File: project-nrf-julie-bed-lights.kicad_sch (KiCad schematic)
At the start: 10 parts

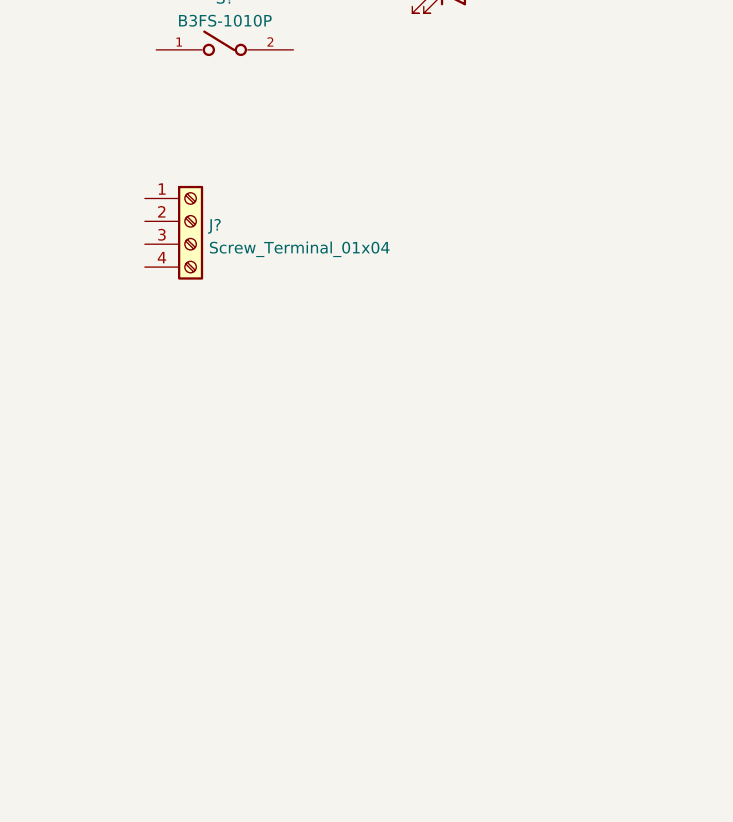
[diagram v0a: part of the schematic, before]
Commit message: Add mounting holes and female sockets
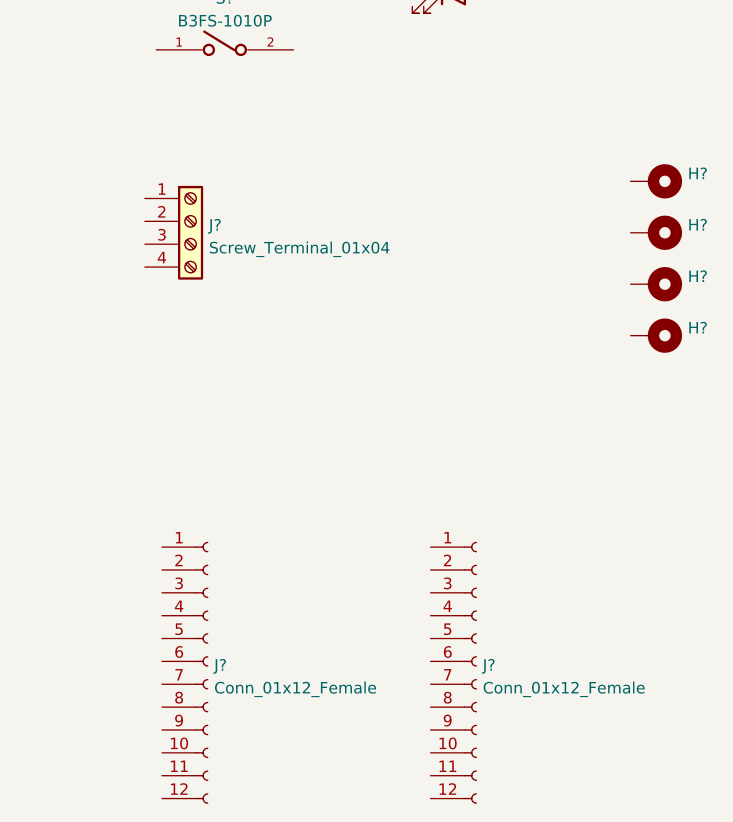
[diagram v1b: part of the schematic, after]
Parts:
- added H? (x4): MountingHole_Pad, MountingHole:MountingHole_2.7mm_M2.5_ISO7380_Pad, symbol Mechanical:MountingHole_Pad
- added J? (x2): Conn_01x12_Female, Connector_PinSocket_2.54mm:PinSocket_1x12_P2.54mm_Vertical_SMD_Pin1Right, symbol Connector:Conn_01x12_Female
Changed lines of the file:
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@@
     (pin "3")
+  )
+  (symbol (lib_id "Mechanical:MountingHole_Pad") (at 149.225 90.17 270) (unit 1)
+    (in_bom yes) (on_board yes) (fields_autoplaced)
+    (property "Reference" "H?" (id 0) (at 153.035 89.3353 90)
+      (effects (font (size 1.27 1.27)) (justify left))
+    )
+    (property "Value" "MountingHole_Pad" (id 1) (at 153.035 91.8722 90)
+      (effects (font (size 1.27 1.27)) (justify left) hide)
+    )
+    (property "Footprint" "MountingHole:MountingHole_2.7mm_M2.5_ISO7380_Pad" (id 2) (at 149.225 90.17 0)
+      (effects (font (size 1.27 1.27)) hide)
+    )
+    (property "Datasheet" "~" (id 3) (at 149.225 90.17 0)
+      (effects (font (size 1.27 1.27)) hide)
+    )
+    (pin "1")
+  )
+  (symbol (lib_id "Connector:Conn_01x12_Female") (at 129.54 137.795 0) (unit 1)
+    (in_bom yes) (on_board yes) (fields_autoplaced)
+    (property "Reference" "J?" (id 0) (at 130.2512 138.2303 0)
+      (effects (font (size 1.27 1.27)) (justify left))
+    )
+    (property "Value" "Conn_01x12_Female" (id 1) (at 130.2512 140.7672 0)
+      (effects (font (size 1.27 1.27)) (justify left))
+    )
+    (property "Footprint" "Connector_PinSocket_2.54mm:PinSocket_1x12_P2.54mm_Vertical_SMD_Pin1Right" (id 2) (at 129.54 137.795 0)
+      (effects (font (size 1.27 1.27)) hide)
+    )
+    (property "Datasheet" "~" (id 3) (at 129.54 137.795 0)
+      (effects (font (size 1.27 1.27)) hide)
+    )
+    (pin "1")
+    (pin "10")
+    (pin "11")
+    (pin "12")
+    (pin "2")
+    (pin "3")
+    (pin "4")
+    (pin "5")
+    (pin "6")
+    (pin "7")
+    (pin "8")
+    (pin "9")
   )
   (symbol (lib_id "Device:LED") (at 127 63.5 0) (unit 1)
@@
     (pin "2")
   )
+  (symbol (lib_id "Mechanical:MountingHole_Pad") (at 149.225 84.455 270) (unit 1)
+    (in_bom yes) (on_board yes) (fields_autoplaced)
+    (property "Reference" "H?" (id 0) (at 153.035 83.6203 90)
+      (effects (font (size 1.27 1.27)) (justify left))
+    )
+    (property "Value" "MountingHole_Pad" (id 1) (at 153.035 86.1572 90)
+      (effects (font (size 1.27 1.27)) (justify left) hide)
+    )
+    (property "Footprint" "MountingHole:MountingHole_2.7mm_M2.5_ISO7380_Pad" (id 2) (at 149.225 84.455 0)
+      (effects (font (size 1.27 1.27)) hide)
+    )
+    (property "Datasheet" "~" (id 3) (at 149.225 84.455 0)
+      (effects (font (size 1.27 1.27)) hide)
+    )
+    (pin "1")
+  )
+  (symbol (lib_id "Mechanical:MountingHole_Pad") (at 149.225 101.6 270) (unit 1)
+    (in_bom yes) (on_board yes) (fields_autoplaced)
+    (property "Reference" "H?" (id 0) (at 153.035 100.7653 90)
+      (effects (font (size 1.27 1.27)) (justify left))
+    )
+    (property "Value" "MountingHole_Pad" (id 1) (at 153.035 103.3022 90)
+      (effects (font (size 1.27 1.27)) (justify left) hide)
+    )
+    (property "Footprint" "MountingHole:MountingHole_2.7mm_M2.5_ISO7380_Pad" (id 2) (at 149.225 101.6 0)
+      (effects (font (size 1.27 1.27)) hide)
+    )
+    (property "Datasheet" "~" (id 3) (at 149.225 101.6 0)
+      (effects (font (size 1.27 1.27)) hide)
+    )
+    (pin "1")
+  )
+  (symbol (lib_id "Mechanical:MountingHole_Pad") (at 149.225 95.885 270) (unit 1)
+    (in_bom yes) (on_board yes) (fields_autoplaced)
+    (property "Reference" "H?" (id 0) (at 153.035 95.0503 90)
+      (effects (font (size 1.27 1.27)) (justify left))
+    )
+    (property "Value" "MountingHole_Pad" (id 1) (at 153.035 97.5872 90)
+      (effects (font (size 1.27 1.27)) (justify left) hide)
+    )
+    (property "Footprint" "MountingHole:MountingHole_2.7mm_M2.5_ISO7380_Pad" (id 2) (at 149.225 95.885 0)
+      (effects (font (size 1.27 1.27)) hide)
+    )
+    (property "Datasheet" "~" (id 3) (at 149.225 95.885 0)
+      (effects (font (size 1.27 1.27)) hide)
+    )
+    (pin "1")
+  )
   (symbol (lib_id "Connector:Screw_Terminal_01x04") (at 97.79 88.9 0) (unit 1)
     (in_bom yes) (on_board yes) (fields_autoplaced)
@@
     (pin "3")
     (pin "4")
+  )
+  (symbol (lib_id "Connector:Conn_01x12_Female") (at 99.695 137.795 0) (unit 1)
+    (in_bom yes) (on_board yes) (fields_autoplaced)
+    (property "Reference" "J?" (id 0) (at 100.4062 138.2303 0)
+      (effects (font (size 1.27 1.27)) (justify left))
+    )
+    (property "Value" "Conn_01x12_Female" (id 1) (at 100.4062 140.7672 0)
+      (effects (font (size 1.27 1.27)) (justify left))
+    )
+    (property "Footprint" "Connector_PinSocket_2.54mm:PinSocket_1x12_P2.54mm_Vertical_SMD_Pin1Right" (id 2) (at 99.695 137.795 0)
+      (effects (font (size 1.27 1.27)) hide)
+    )
+    (property "Datasheet" "~" (id 3) (at 99.695 137.795 0)
+      (effects (font (size 1.27 1.27)) hide)
+    )
+    (pin "1")
+    (pin "10")
+    (pin "11")
+    (pin "12")
+    (pin "2")
+    (pin "3")
+    (pin "4")
+    (pin "5")
+    (pin "6")
+    (pin "7")
+    (pin "8")
+    (pin "9")
   )
   (symbol (lib_id "Device:LED") (at 127 53.34 0) (unit 1)
@@
       (reference "D?") (unit 1) (value "Color") (footprint "LED_SMD:LED_0603_1608Metric")
     )
+    (path "/79a1a979-e26f-4163-9550-e2360d22044b"
+      (reference "H?") (unit 1) (value "MountingHole_Pad") (footprint "MountingHole:MountingHole_2.7mm_M2.5_ISO7380_Pad")
+    )
+    (path "/ad7a890b-9961-45f3-ad0a-47d76a2b459a"
+      (reference "H?") (unit 1) (value "MountingHole_Pad") (footprint "MountingHole:MountingHole_2.7mm_M2.5_ISO7380_Pad")
+    )
+    (path "/b87d5433-df83-465a-b91e-7e1ece85c8fe"
+      (reference "H?") (unit 1) (value "MountingHole_Pad") (footprint "MountingHole:MountingHole_2.7mm_M2.5_ISO7380_Pad")
+    )
+    (path "/d2b03c54-b52a-42dc-b552-8744a7b0080b"
+      (reference "H?") (unit 1) (value "MountingHole_Pad") (footprint "MountingHole:MountingHole_2.7mm_M2.5_ISO7380_Pad")
+    )
     (path "/384cfa91-ee4e-4e2d-8fc4-bda226af1052"
       (reference "J?") (unit 1) (value "PJ-036AH-SMT-TR") (footprint "PJ-036AH-SMT-TR:CUI_PJ-036AH-SMT-TR")
     )
+    (path "/93480494-31ee-42ec-b157-ad9a7625797b"
+      (reference "J?") (unit 1) (value "Conn_01x12_Female") (footprint "Connector_PinSocket_2.54mm:PinSocket_1x12_P2.54mm_Vertical_SMD_Pin1Right")
+    )
     (path "/d4522741-f06b-485a-8c53-80d199b4eb97"
       (reference "J?") (unit 1) (value "Screw_Terminal_01x04") (footprint "TZ042101B000G:TZ042101B000G")
     )
+    (path "/d6cb7b6b-2ea2-4533-af54-c8714717f7a9"
+      (reference "J?") (unit 1) (value "Conn_01x12_Female") (footprint "Connector_PinSocket_2.54mm:PinSocket_1x12_P2.54mm_Vertical_SMD_Pin1Right")
+    )
     (path "/2c6b9ce7-e37f-44db-b118-82a9f4da9904"

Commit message: Half the schematic ready
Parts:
- removed Q? (x2): Si2312BDS, Package_TO_SOT_SMD:SOT-23, symbol Device:Q_NMOS_GSD
- removed U?: LP2985-50DBVR, LP2985-50:SOT95P280X145-5N, symbol LP2985-50DBVR:LP2985-50DBVR
- added C?: 100nF, Capacitor_SMD:C_0603_1608Metric, symbol Device:C
- added C?: 10uF, Capacitor_SMD:C_0805_2012Metric, symbol Device:C
- added C?: 22uF, Capacitor_SMD:C_0805_2012Metric, symbol Device:C
- added C?: DNI, Capacitor_SMD:C_0603_1608Metric, symbol Device:C
- added L?: 10uH, LBR2518T100K:INDC2518X200N, symbol LBR2518T100K:LBR2518T100K
- added Q? (x2): RU1J002YN, Package_TO_SOT_SMD:SOT-323_SC-70, symbol Device:Q_NMOS_GSD
- added Q? (x2): Si231BDS, Package_TO_SOT_SMD:SOT-23, symbol Device:Q_NMOS_GSD
- added R? (x7): 10k, Resistor_SMD:R_0603_1608Metric, symbol Device:R
- added R?: 30.1k, Resistor_SMD:R_0603_1608Metric, symbol Device:R
- added R?: 37.4k, Resistor_SMD:R_0603_1608Metric, symbol Device:R
- added U?: AP63300WU-7, AP63300WU-7:SOT95P280X100-6N, symbol AP63300WU-7:AP63300WU-7
- Q?: value Si2312BDS -> Si231BDS
- S?: value B3FS-1010P -> Change mode
- SW?: value RotaryEncoder_Switch -> Change value; footprint (none) -> PEC11S-9213K-S0015:PEC11S-9213K-S0015
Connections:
- net GND: now reaches SW?.S2
- net GND: now also H?.1, H?.1, H?.1, H?.1, J?.2, Q?.2 (S), S?.2, C?.2, C?.2, Q?.2 (S), Q?.2 (S), Q?.2 (S), Q?.2 (S), R?.2, R?.2, R?.2, R?.2, R?.2, R?.2, U?.4 (GND)
- net at Q?.1 (G): now also R?.1
- net Bleu: now reaches Q?.3 (D)
- net Bleu: now also J?.2 (Pin_2)
- net +12V: now reaches J?.1
- net +12V: now also J?.1 (Pin_1), C?.1, R?.1, R?.1, U?.2 (EN), U?.3 (VIN)
- net at D?.1 (K): now also Q?.3 (D) (x2)
- net at D?.2 (A): now also R?.2 (x2)
- net Rouge: now reaches J?.3 (Pin_3)
- net Rouge: now also Q?.3 (D)
- net Vert: now reaches J?.4 (Pin_4)
- net Vert: now also Q?.3 (D)
- new net: C?.1, L?.1, U?.5 (SW)
- new net: C?.2, U?.6 (BST)
- new net: Q?.1 (G), R?.1 (x4)
- new net: C?.2, R?.1, R?.2, U?.1 (FB)
- new net +1V8: C?.1, C?.1, L?.2, R?.1
- no-connect marks 0 -> 1
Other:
- moved on the sheet: D?, H?, J?, Q?, S?, SW?

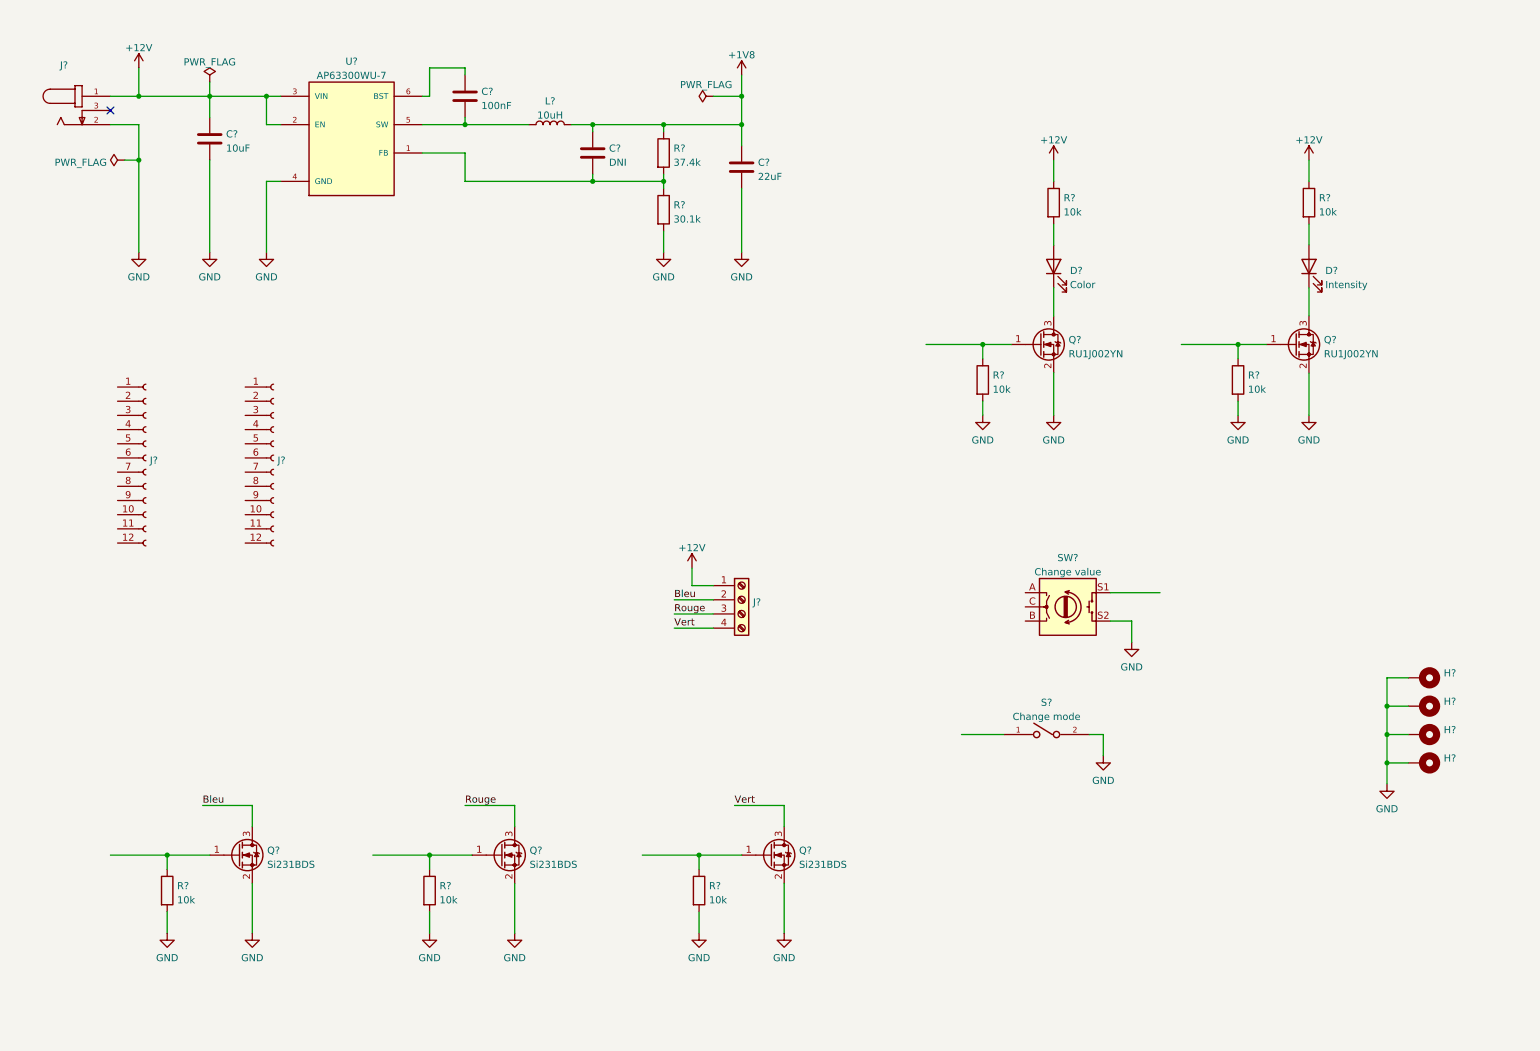
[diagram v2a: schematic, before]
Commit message: Add the pink_panda sub-sheet
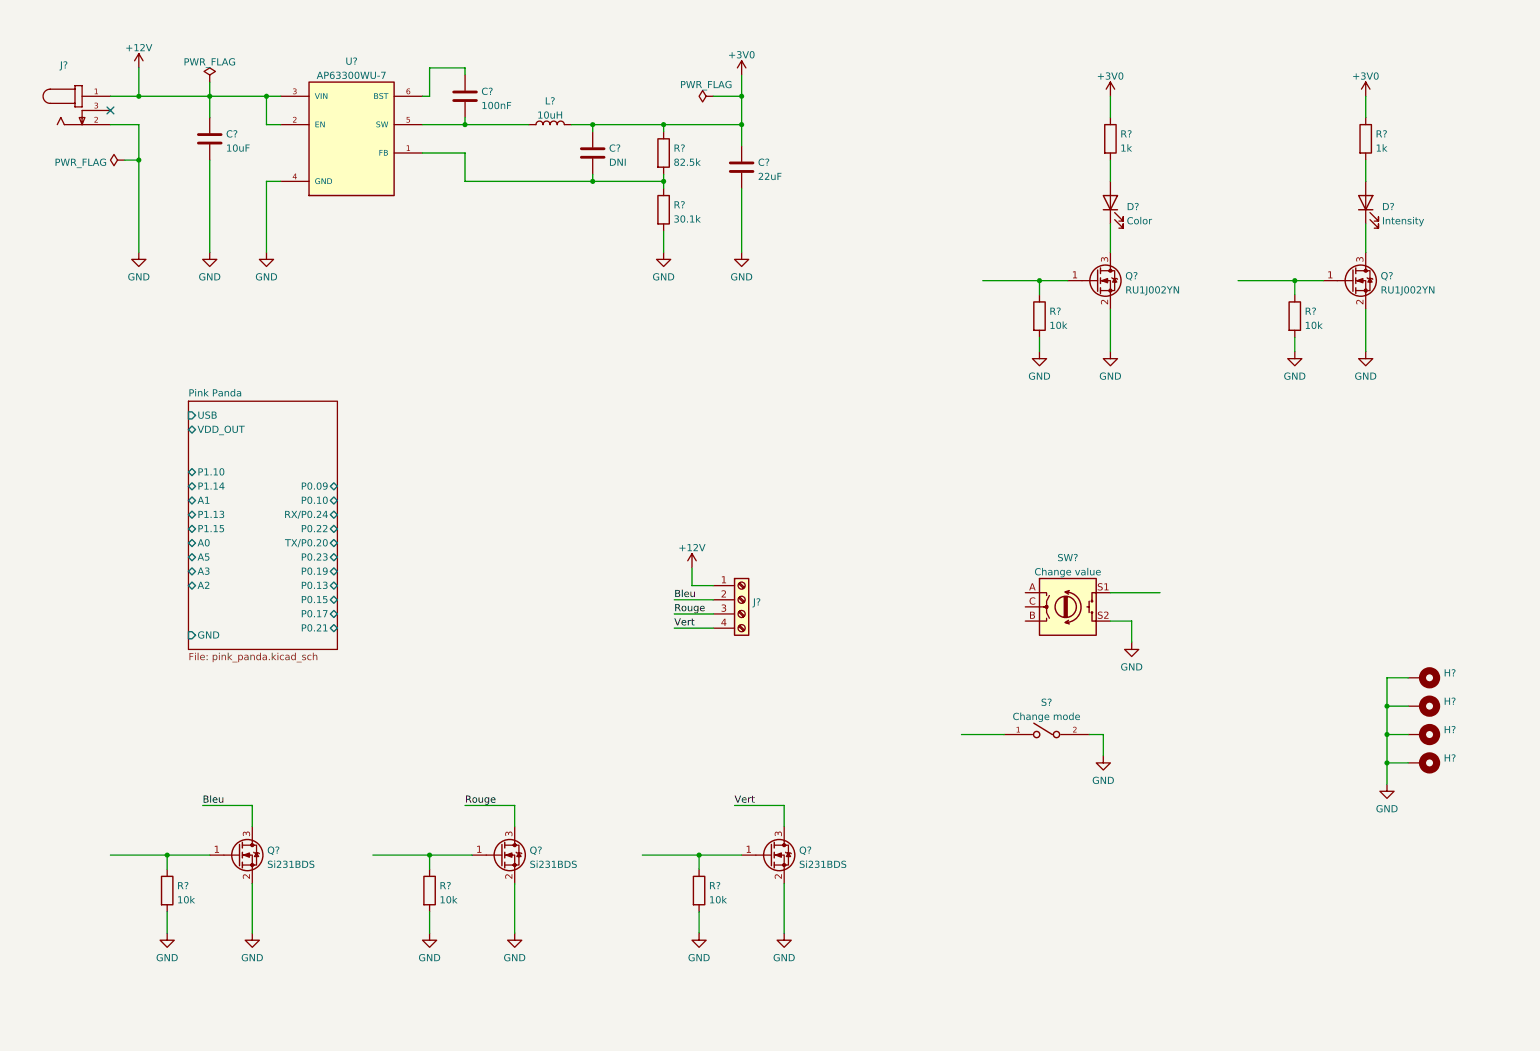
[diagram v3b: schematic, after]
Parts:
- removed J? (x2): Conn_01x12_Female, Connector_PinSocket_2.54mm:PinSocket_1x12_P2.54mm_Vertical_SMD_Pin1Right, symbol Connector:Conn_01x12_Female
- R?: value 37.4k -> 82.5k
- R? (x2): value 10k -> 1k
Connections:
- net +12V: no longer R?.1, R?.1
- net +1V8 renamed +3V0
- net +3V0: now also R?.1, R?.1
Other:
- added sheet Pink Panda (pink_panda.kicad_sch)
- moved on the sheet: D?, Q?, R?

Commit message: Connect everything to the panda board
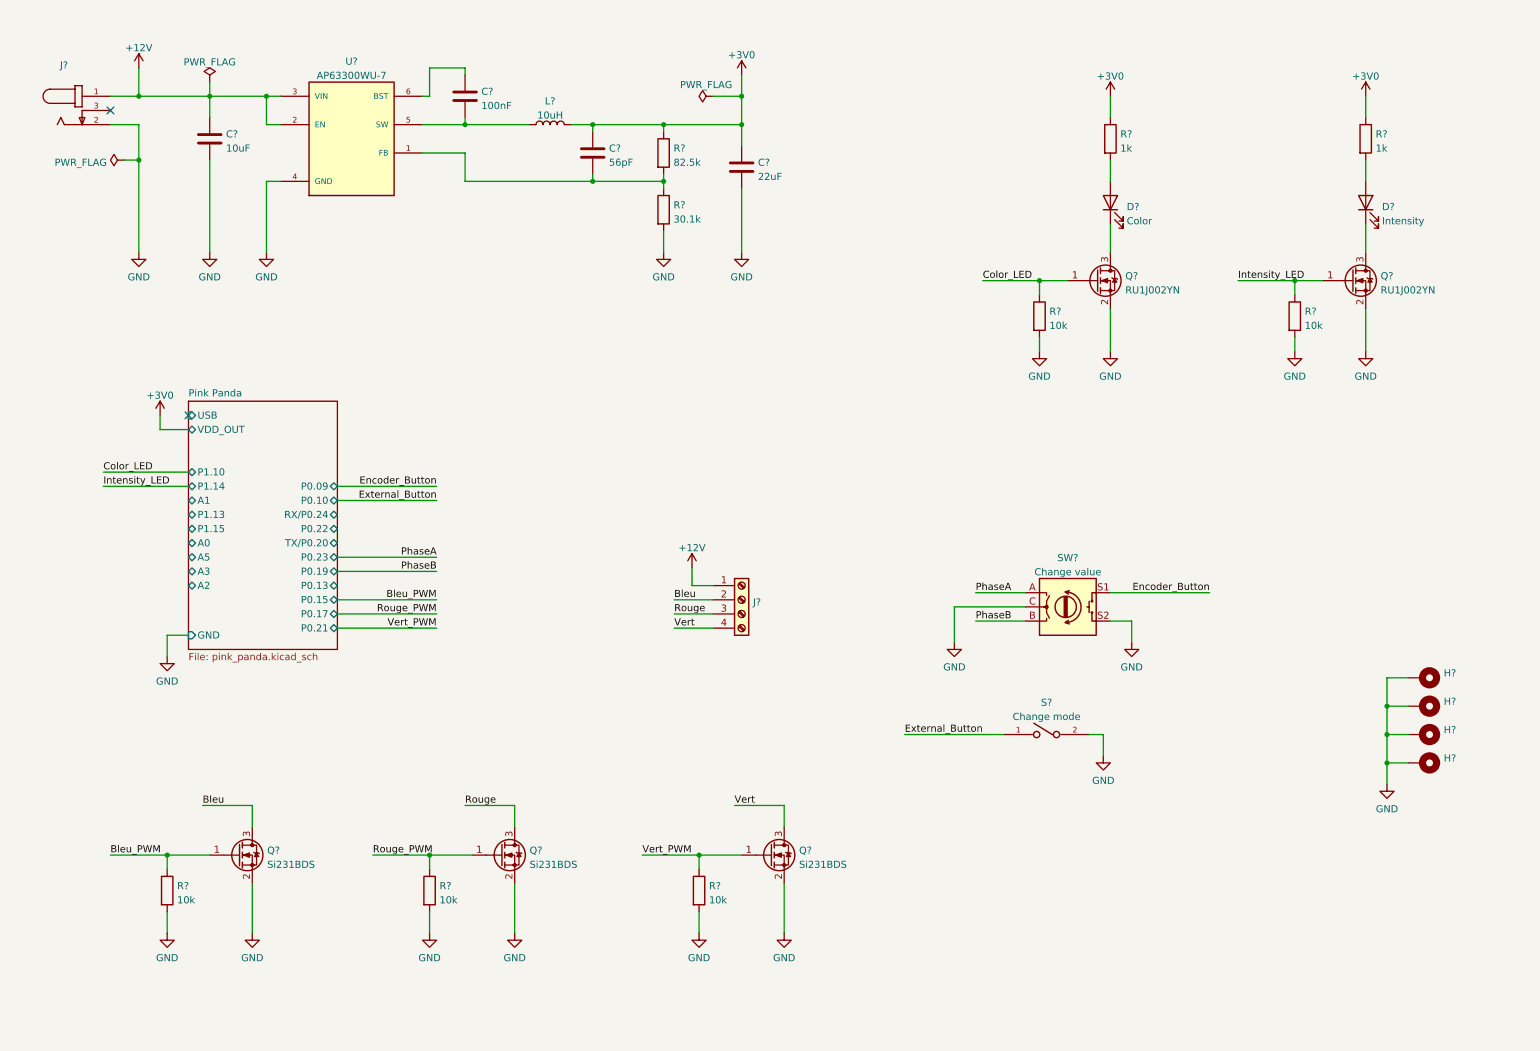
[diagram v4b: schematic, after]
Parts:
- C?: value DNI -> 56pF
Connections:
- net GND: now also SW?.C
- net Intensity_LED: now reaches Q?.1 (G), R?.1
- net PhaseA: now reaches SW?.A
- net PhaseB: now reaches SW?.B
- net Encoder_Button: now reaches SW?.S1
- net Bleu_PWM: now reaches Q?.1 (G), R?.1
- net Color_LED: now reaches Q?.1 (G), R?.1
- net External_Button: now reaches S?.1
- net Vert_PWM: now reaches Q?.1 (G), R?.1
- net Rouge_PWM: now reaches Q?.1 (G), R?.1
- no-connect marks 1 -> 2
